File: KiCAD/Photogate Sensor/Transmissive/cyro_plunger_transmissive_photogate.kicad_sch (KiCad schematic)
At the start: 47 parts, among them J1 FFC, J2 FFC Socket, J3 USB_B_Micro, J4 UPDI socket, J6 Conn_01x03_Socket, Q1 Q_NMOS_GSD, Q2 Q_NMOS_GSD, Q3 Q_NMOS_GSD, Q4 Q_NMOS_GSD, U1 5V LDO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

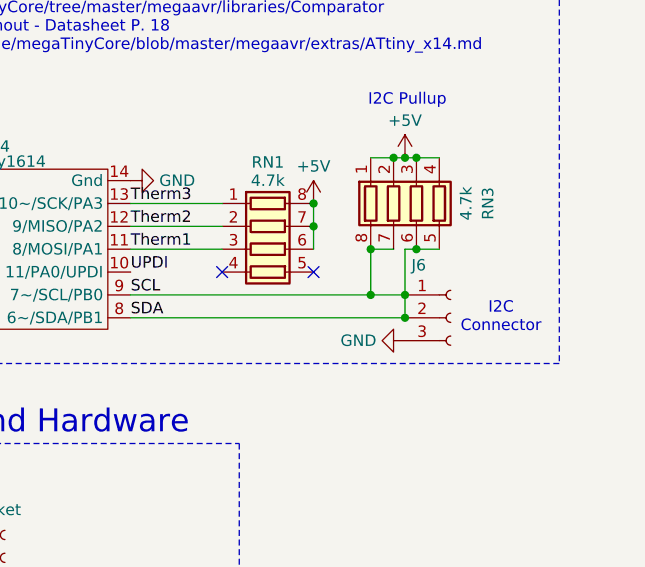
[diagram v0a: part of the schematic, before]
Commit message: Thermally isolated heaters
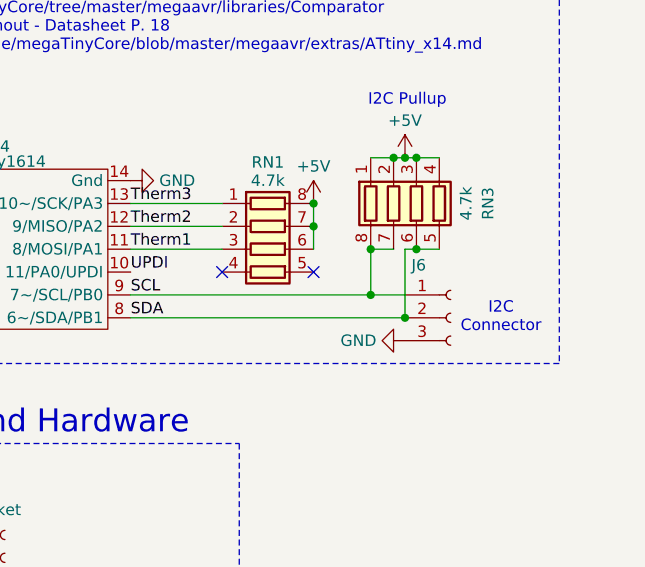
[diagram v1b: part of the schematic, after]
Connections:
- net SCL: no longer J6.2 (Pin_2), RN3.5 (R4.2), RN3.6 (R3.2), U3.8 (SDA), U4.8 (6~/SDA/PB1)
- new net SDA: J6.2 (Pin_2), RN3.5 (R4.2), RN3.6 (R3.2), U3.8 (SDA), U4.8 (6~/SDA/PB1)
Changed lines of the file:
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@@
-	)
-	(junction
-		(at 264.16 110.49)
-		(diameter 0)
-		(color 0 0 0 0)
 	)
 	(junction
@@
 	(wire
 		(pts
-			(xy 264.16 110.49) (xy 264.16 113.03)
+			(xy 264.16 105.41) (xy 264.16 113.03)
 		)
 		(stroke
@@
 		)
 		(stroke
-			(width 0)
-			(type default)
-		)
-	)
-	(wire
-		(pts
-			(xy 264.16 105.41) (xy 264.16 110.49)
-		)
-		(stroke

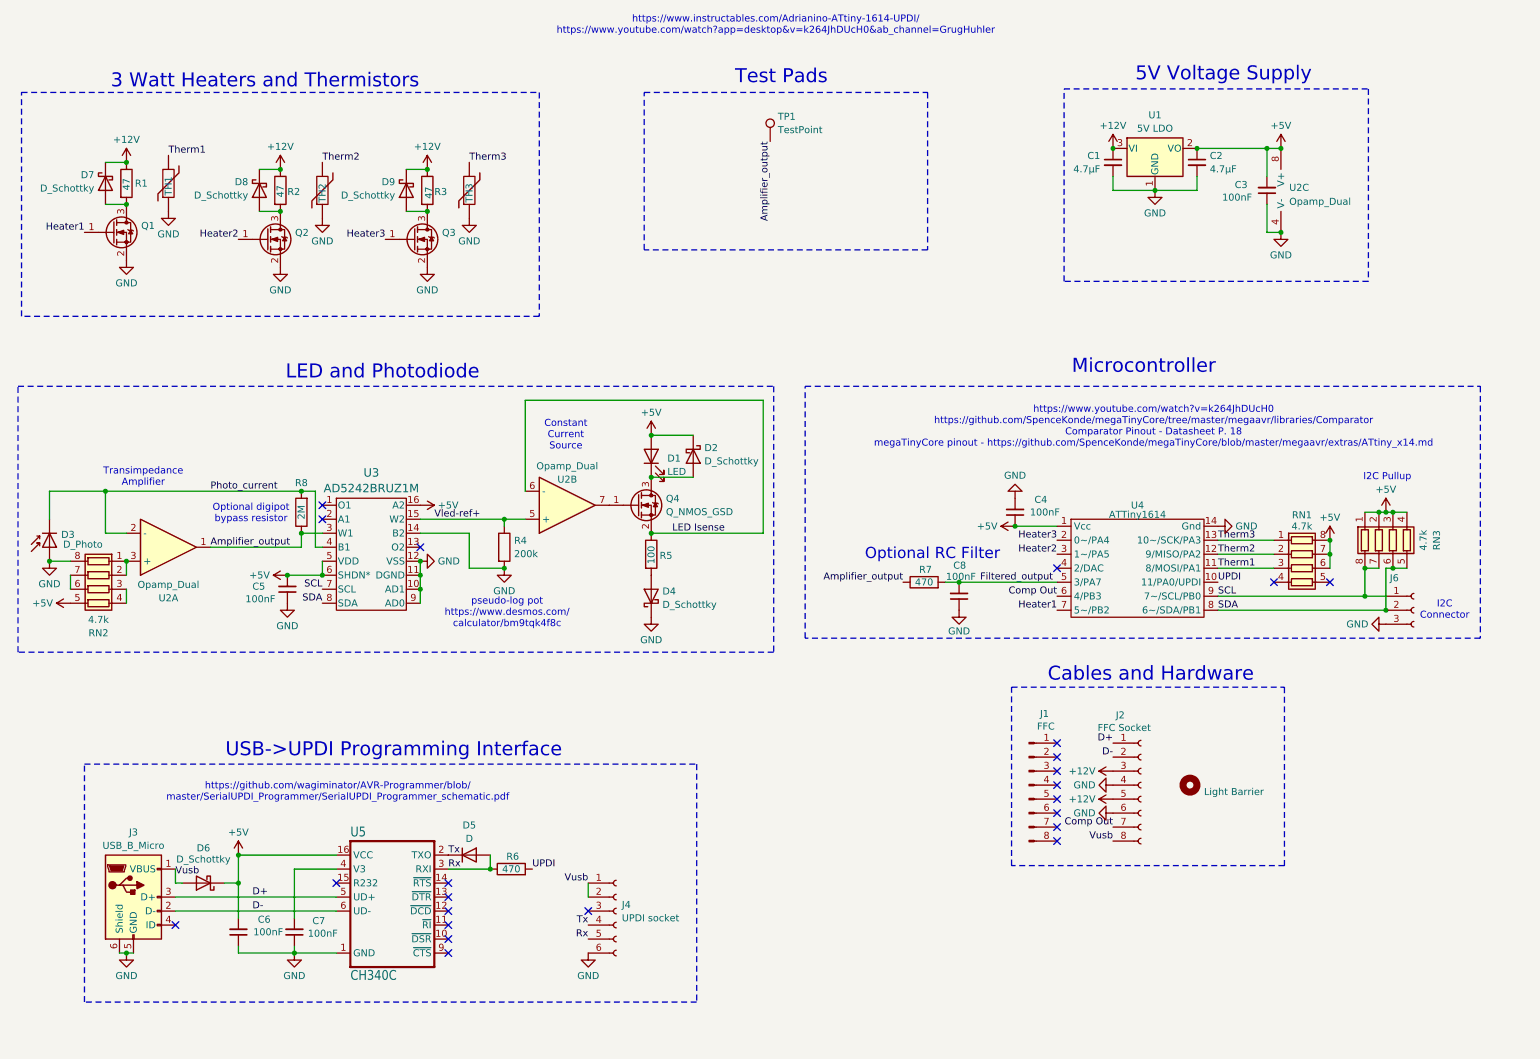
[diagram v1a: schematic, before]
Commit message: connection board wired and skew matched
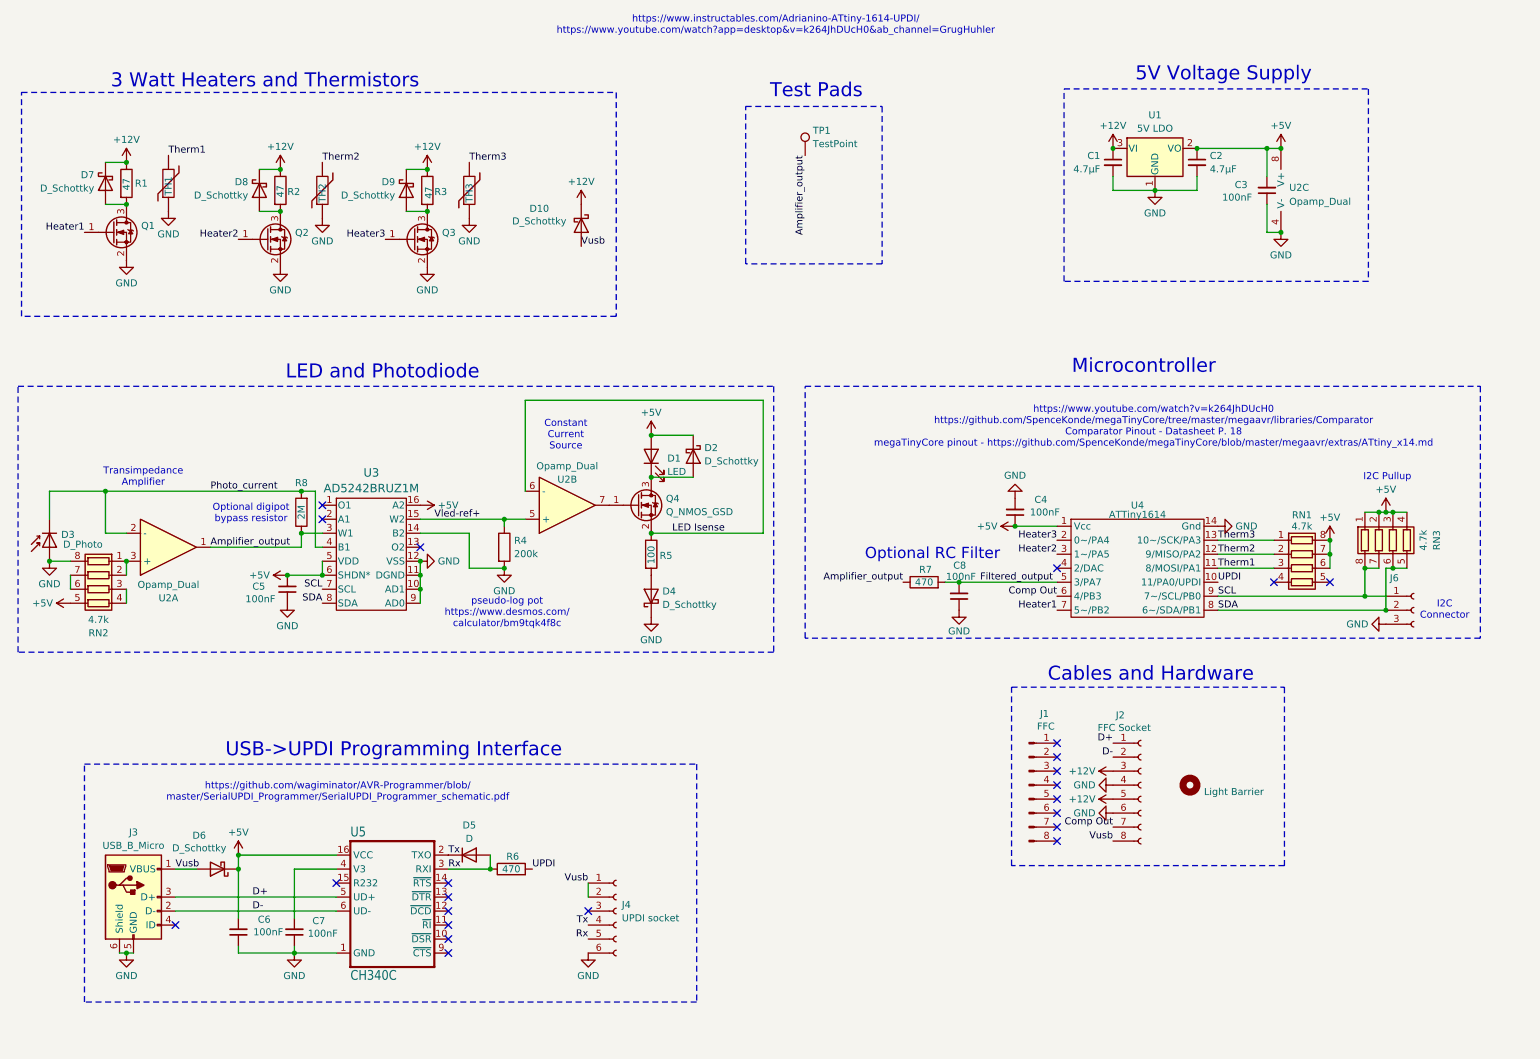
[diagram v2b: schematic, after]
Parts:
- added D10: D_Schottky, Diode_SMD:D_SOD-323, symbol Device:D_Schottky
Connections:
- net +12V: now also D10.1 (K)
- net Vusb: now also D10.2 (A)
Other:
- moved on the sheet: D6, TP1
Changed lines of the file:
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@@
 	)
 	(junction
-		(at 55.88 162.56)
-		(diameter 0)
-		(color 0 0 0 0)
-	)
-	(junction
 		(at 130.81 88.9)
 		(diameter 0)
@@
 	)
 	(junction
+		(at 55.88 160.02)
+		(diameter 0)
+		(color 0 0 0 0)
+	)
+	(junction
 		(at 63.5 33.02)
 		(diameter 0)
@@
 	(wire
 		(pts
-			(xy 53.34 162.56) (xy 55.88 162.56)
-		)
-		(stroke
-			(width 0)
-			(type default)
-		)
-	)
-	(wire
-		(pts
 			(xy 264.16 95.25) (xy 265.43 95.25)
 		)
@@
 	(wire
 		(pts
-			(xy 55.88 157.48) (xy 55.88 162.56)
+			(xy 55.88 160.02) (xy 55.88 168.91)
+		)
+		(stroke
+			(width 0.1524)
+			(type solid)
+		)
+	)
+	(wire
+		(pts
+			(xy 55.88 157.48) (xy 55.88 160.02)
 		)
 		(stroke
@@
 	(wire
 		(pts
+			(xy 44.45 160.02) (xy 48.26 160.02)
+		)
+		(stroke
+			(width 0)
+			(type default)
+		)
+	)
+	(wire
+		(pts
 			(xy 260.35 105.41) (xy 262.89 105.41)
 		)
@@
 	(wire
 		(pts
-			(xy 44.45 162.56) (xy 45.72 162.56)
-		)
-		(stroke
-			(width 0)
-			(type default)
-		)
-	)
-	(wire
-		(pts
 			(xy 265.43 95.25) (xy 267.97 95.25)
 		)
@@
 	(wire
 		(pts
-			(xy 55.88 162.56) (xy 55.88 168.91)
-		)
-		(stroke
-			(width 0.1524)
-			(type solid)
-		)
-	)
-	(wire
-		(pts
 			(xy 67.31 99.06) (xy 67.31 101.6)
 		)
@@
 	(wire
 		(pts
-			(xy 44.45 160.02) (xy 44.45 162.56)
-		)
-		(stroke
-			(width 0)
-			(type default)
-		)
-	)
-	(wire
-		(pts
 			(xy 35.56 109.22) (xy 35.56 111.76)
 		)
@@
 	)
 	(rectangle
-		(start 129.54 19.05)
-		(end 180.975 47.625)
+		(start 147.955 21.59)
+		(end 172.72 50.165)
 		(stroke
 			(width 0)
@@
 	(rectangle
 		(start 16.51 19.05)
-		(end 110.49 59.69)
+		(end 124.46 59.69)
 		(stroke
 			(width 0)
@@
 	(text "Test Pads"
 		(exclude_from_sim no)
-		(at 154.432 16.256 0)
+		(at 160.782 18.796 0)
 		(effects
 			(font
@@
 		)
 	)
+	(label "Vusb"
+		(at 118.11 46.99 0)
+		(fields_autoplaced yes)
+		(effects
+			(font
+				(size 1.27 1.27)
+			)
+			(justify left bottom)
+		)
+	)
 	(label "LED Isense"
 		(at 134.62 99.06 0)
@@
 	)
 	(label "Vusb"
-		(at 44.45 161.29 0)
+		(at 44.45 160.02 0)
 		(fields_autoplaced yes)
 		(effects
@@
 	)
 	(label "Amplifier_output"
-		(at 152.4 27.94 270)
+		(at 158.75 30.48 270)
 		(fields_autoplaced yes)
 		(effects
@@
 	)
 	(symbol
+		(lib_id "power:+12V")
+		(at 118.11 39.37 0)
+		(unit 1)
+		(exclude_from_sim no)
+		(in_bom yes)
+		(on_board yes)
+		(dnp no)
+		(fields_autoplaced yes)
+		(property "Reference" "#PWR038"
+			(at 118.11 43.18 0)
+			(effects
+				(font
+					(size 1.27 1.27)
+				)
+				(hide yes)
+			)
+		)
+		(property "Value" "+12V"
+			(at 118.11 35.2369 0)
+			(effects
+				(font
+					(size 1.27 1.27)
+				)
+			)
+		)
+		(property "Footprint" ""
+			(at 118.11 39.37 0)
+			(effects
+				(font
+					(size 1.27 1.27)
+				)
+				(hide yes)
+			)
+		)
+		(property "Datasheet" ""
+			(at 118.11 39.37 0)
+			(effects
+				(font
+					(size 1.27 1.27)
+				)
+				(hide yes)
+			)
+		)
+		(property "Description" "Power symbol creates a global label with name \"+12V\""
+			(at 118.11 39.37 0)
+			(effects
+				(font
+					(size 1.27 1.27)
+				)
+				(hide yes)
+			)
+		)
+		(pin "1"
+		)
+		(instances
+			(project "cyro_plunger_transmissive_photogate"
+				(path "/99ca36d5-bbf3-497e-815f-42a5447a2ddc"
+					(reference "#PWR038")
+					(unit 1)
+				)
+			)
+		)
+	)
+	(symbol
 		(lib_id "Device:Thermistor")
 		(at 97.79 36.83 0)
@@
 	(symbol
 		(lib_id "Connector:TestPoint")
-		(at 152.4 27.94 0)
+		(at 158.75 30.48 0)
 		(unit 1)
 		(exclude_from_sim no)
@@
 		(fields_autoplaced yes)
 		(property "Reference" "TP1"
-			(at 153.797 23.4258 0)
+			(at 160.147 25.9658 0)
 			(effects
 				(font
@@
 		)
 		(property "Value" "TestPoint"
-			(at 153.797 25.8501 0)
+			(at 160.147 28.3901 0)
 			(effects
 				(font
@@
 		)
 		(property "Footprint" "Custom:1x Solder pads"
-			(at 157.48 27.94 0)
+			(at 163.83 30.48 0)
 			(effects
 				(font
@@
 		)
 		(property "Datasheet" "~"
-			(at 157.48 27.94 0)
+			(at 163.83 30.48 0)
 			(effects
 				(font
@@
 		)
 		(property "Description" "test point"
-			(at 152.4 27.94 0)
+			(at 158.75 30.48 0)
 			(effects
 				(font
@@
 		)
 		(property "Manufacturer" ""
-			(at 152.4 27.94 0)
+			(at 158.75 30.48 0)
 			(effects
 				(font
@@
 		)
 		(property "Part" ""
-			(at 152.4 27.94 0)
+			(at 158.75 30.48 0)
 			(effects
 				(font
@@
 	(symbol
 		(lib_id "Device:D_Schottky")
-		(at 49.53 162.56 180)
+		(at 52.07 160.02 180)
 		(unit 1)
 		(exclude_from_sim no)
@@
 		(dnp no)
 		(property "Reference" "D6"
-			(at 49.53 156.21 0)
+			(at 48.768 153.924 0)
 			(effects
 				(font
@@
 		)
 		(property "Value" "D_Schottky"
-			(at 49.53 158.242 0)
+			(at 48.768 156.21 0)
 			(effects
 				(font
@@
 		)
 		(property "Footprint" "Diode_SMD:D_SOD-323"
-			(at 49.53 162.56 0)
+			(at 52.07 160.02 0)
 			(effects
 				(font
@@
 		)
 		(property "Datasheet" "https://toshiba.semicon-storage.com/info/docget.jsp?did=14077&prodName=CUS10S30"
-			(at 49.53 162.56 0)
+			(at 52.07 160.02 0)
 			(effects
 				(font
@@
 		)
 		(property "Description" "Diode 30 V 1A Surface Mount USC"
-			(at 49.53 162.56 0)
+			(at 52.07 160.02 0)
 			(effects
 				(font
@@
 		)
 		(property "Manufacturer" "Toshiba Semiconductor and Storage"
-			(at 49.53 162.56 0)
+			(at 52.07 160.02 0)
 			(effects
 				(font
@@
 		)
 		(property "Part" "CUS10S30,H3F"
-			(at 49.53 162.56 0)
+			(at 52.07 160.02 0)
 			(effects
 				(font
@@
 					(unit 1)
 				)
+			)
+		)
+	)
+	(symbol
+		(lib_id "Device:D_Schottky")
+		(at 118.11 43.18 270)
+		(unit 1)
+		(exclude_from_sim no)
+		(in_bom yes)
+		(on_board yes)
+		(dnp no)
+		(property "Reference" "D10"
+			(at 110.49 40.132 90)
+			(effects
+				(font
+					(size 1.27 1.27)
+				)
+			)
+		)
+		(property "Value" "D_Schottky"
+			(at 110.49 42.418 90)
+			(effects
+				(font
+					(size 1.27 1.27)
+				)
+			)
+		)
+		(property "Footprint" "Diode_SMD:D_SOD-323"
+			(at 118.11 43.18 0)
+			(effects
+				(font
+					(size 1.27 1.27)
+				)
+				(hide yes)
+			)
+		)
+		(property "Datasheet" "https://toshiba.semicon-storage.com/info/docget.jsp?did=14077&prodName=CUS10S30"
+			(at 118.11 43.18 0)
+			(effects
+				(font
+					(size 1.27 1.27)
+				)
+				(hide yes)
+			)
+		)
+		(property "Description" "Diode 30 V 1A Surface Mount USC"
+			(at 118.11 43.18 0)
+			(effects
+				(font
+					(size 1.27 1.27)
+				)
+				(hide yes)
+			)
+		)
+		(property "Manufacturer" "Toshiba Semiconductor and Storage"
+			(at 118.11 43.18 0)
+			(effects
+				(font
+					(size 1.27 1.27)
+				)
+				(hide yes)
+			)
+		)
+		(property "Part" "CUS10S30,H3F"
+			(at 118.11 43.18 0)
+			(effects
+				(font
+					(size 1.27 1.27)
+				)
+				(hide yes)
+			)
+		)
+		(pin "1"
+		)
+		(pin "2"
+		)
+		(instances
+			(project "cyro_plunger_transmissive_photogate"
+				(path "/99ca36d5-bbf3-497e-815f-42a5447a2ddc"
+					(reference "D10")
+					(unit 1)
+				)

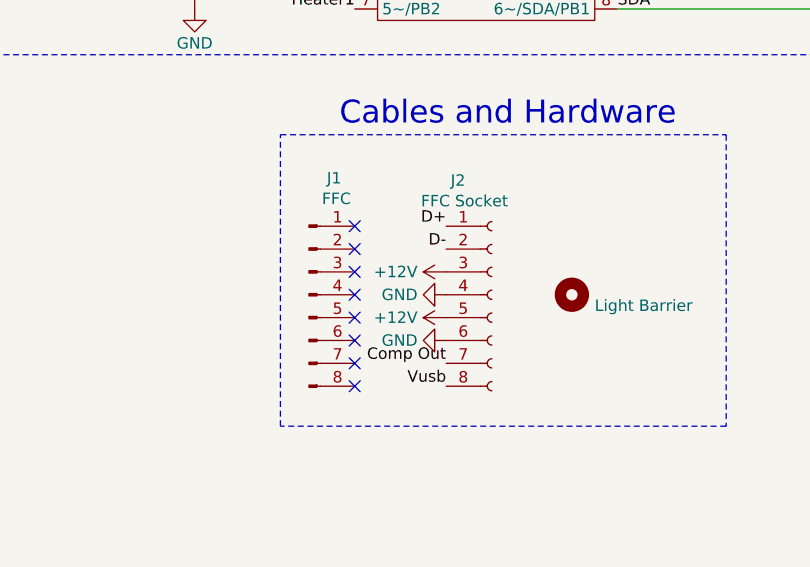
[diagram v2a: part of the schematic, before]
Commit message: Place Gnds closer to data lines on FFC
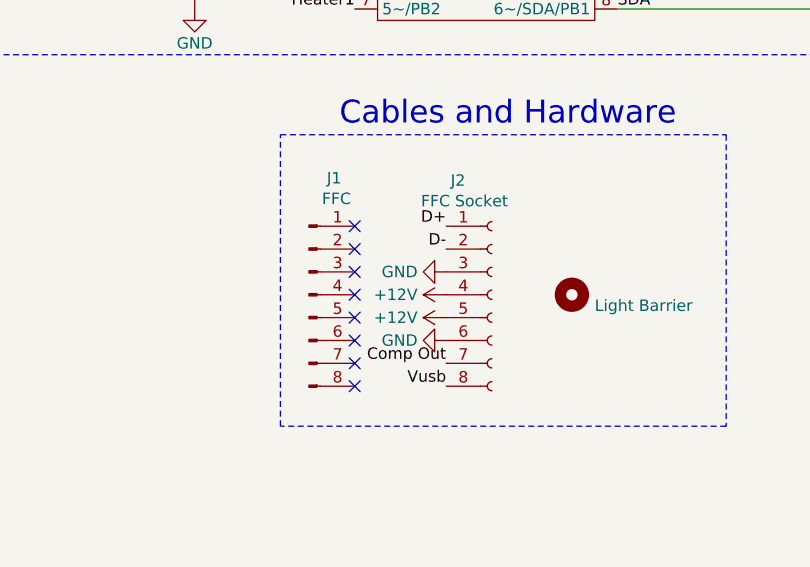
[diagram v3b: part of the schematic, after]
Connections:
- net +12V: now also J2.4 (Pin_4); no longer J2.3 (Pin_3)
- net GND: now also J2.3 (Pin_3); no longer J2.4 (Pin_4)
